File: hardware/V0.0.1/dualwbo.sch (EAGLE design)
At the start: 93 parts, among them IC1 AT90CAN128, IC10 ADS1015BQDGSRQ1, IC11 AD5337BRMZ, IC12 ADS1015BQDGSRQ1, IC2 AVR-JTAG, IC3 TJA1050, IC4 ADR01_02_03, IC5 TLS115B0EJXUMA1, IC6 TLE42754D, IC7 CJ125_QFP32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

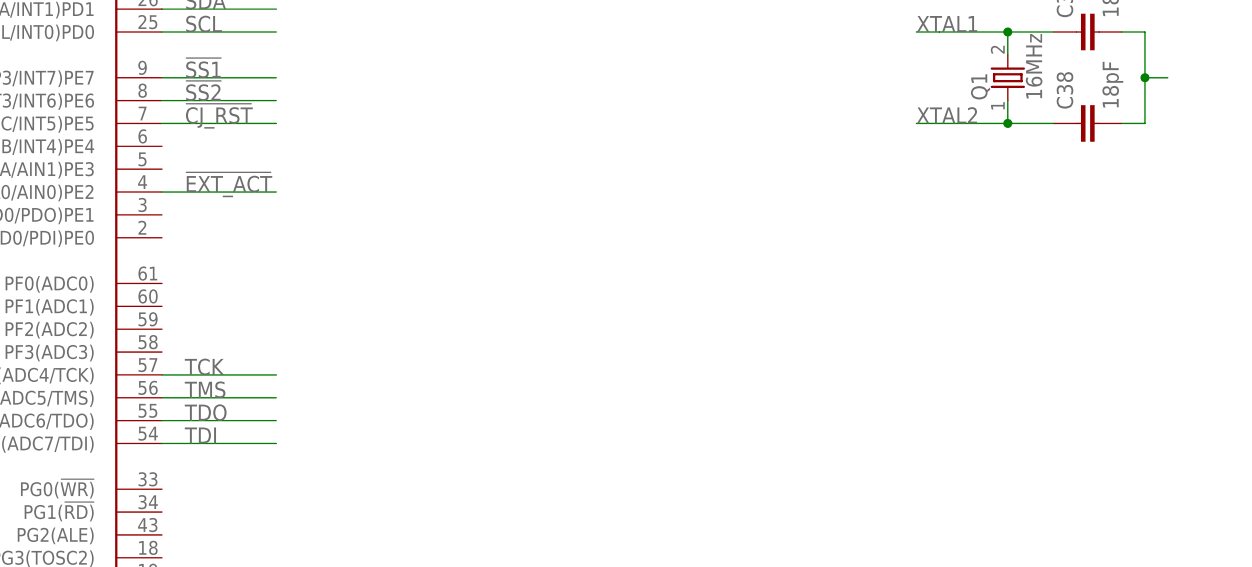
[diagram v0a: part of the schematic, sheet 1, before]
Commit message: uart added
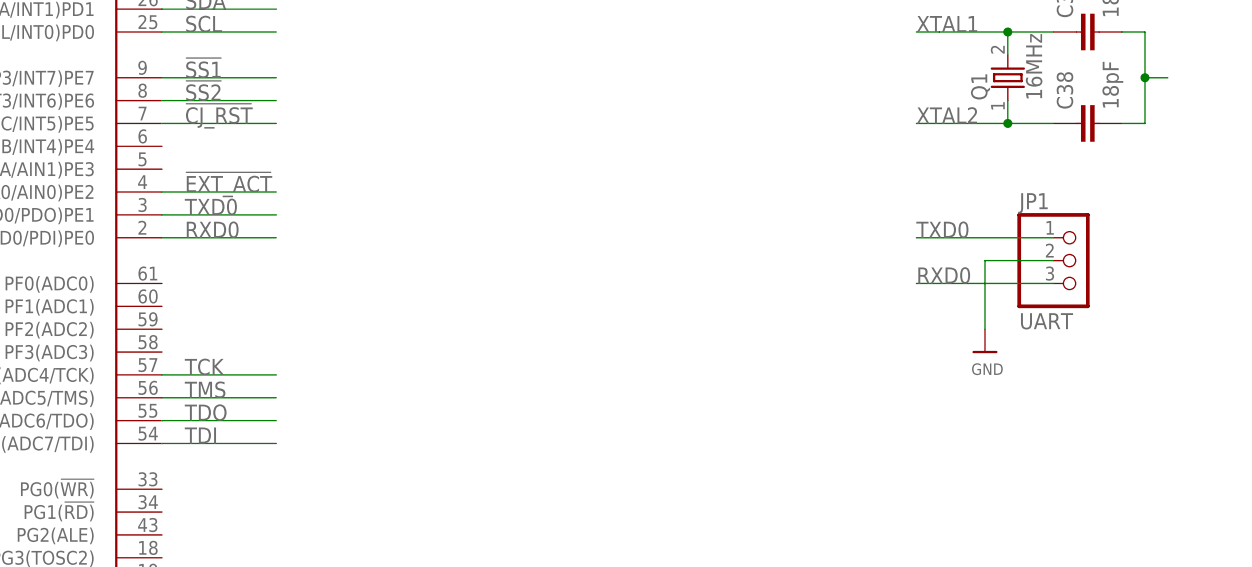
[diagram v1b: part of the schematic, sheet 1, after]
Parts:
- added JP1: UART, Heinrich:PINHD-1X3
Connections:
- new net RXD0: IC1.(RXD0/PDI)PE0, JP1.3
- new net TXD0: IC1.(TXD0/PDO)PE1, JP1.1
- net GND: now also JP1.2
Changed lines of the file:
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@@
 <part name="C40" library="rcl" library_urn="urn:adsk.eagle:library:334" deviceset="C-EU" device="C0805" package3d_urn="urn:adsk.eagle:package:23617/2" value="1uF"/>
 <part name="U$72" library="microbuilder" deviceset="AGND" device=""/>
+<part name="JP1" library="Heinrich" deviceset="PINHD-1X3" device="" value="UART"/>
+<part name="U$82" library="microbuilder" deviceset="GND" device=""/>
 </parts>
 <sheets>
@@
 <instance part="C6" gate="G$1" x="27.94" y="139.7"/>
 <instance part="U$77" gate="G$1" x="27.94" y="129.54"/>
+<instance part="JP1" gate="G$1" x="215.9" y="53.34"/>
+<instance part="U$82" gate="G$1" x="208.28" y="40.64"/>
 </instances>
 <busses>
@@
 <pinref part="U$4" gate="G$1" pin="GND"/>
 <wire x1="220.98" y1="121.92" x2="220.98" y2="119.38" width="0.1524" layer="91"/>
+</segment>
+<segment>
+<pinref part="JP1" gate="G$1" pin="2"/>
+<wire x1="215.9" y1="50.8" x2="208.28" y2="50.8" width="0.1524" layer="91"/>
+<wire x1="208.28" y1="50.8" x2="208.28" y2="43.18" width="0.1524" layer="91"/>
+<pinref part="U$82" gate="G$1" pin="GND"/>
 </segment>
 </net>
@@
 </segment>
 </net>
+<net name="TXD0" class="0">
+<segment>
+<pinref part="IC1" gate="G$1" pin="(TXD0/PDO)PE1"/>
+<wire x1="116.84" y1="55.88" x2="129.54" y2="55.88" width="0.1524" layer="91"/>
+<label x="119.38" y="55.88" size="1.778" layer="95"/>
+</segment>
+<segment>
+<pinref part="JP1" gate="G$1" pin="1"/>
+<wire x1="215.9" y1="53.34" x2="200.66" y2="53.34" width="0.1524" layer="91"/>
+<label x="200.66" y="53.34" size="1.778" layer="95"/>
+</segment>
+</net>
+<net name="RXD0" class="0">
+<segment>
+<pinref part="IC1" gate="G$1" pin="(RXD0/PDI)PE0"/>
+<wire x1="116.84" y1="53.34" x2="129.54" y2="53.34" width="0.1524" layer="91"/>
+<label x="119.38" y="53.34" size="1.778" layer="95"/>
+</segment>
+<segment>
+<pinref part="JP1" gate="G$1" pin="3"/>
+<wire x1="215.9" y1="48.26" x2="200.66" y2="48.26" width="0.1524" layer="91"/>
+<label x="200.66" y="48.26" size="1.778" layer="95"/>
+</segment>
+</net>

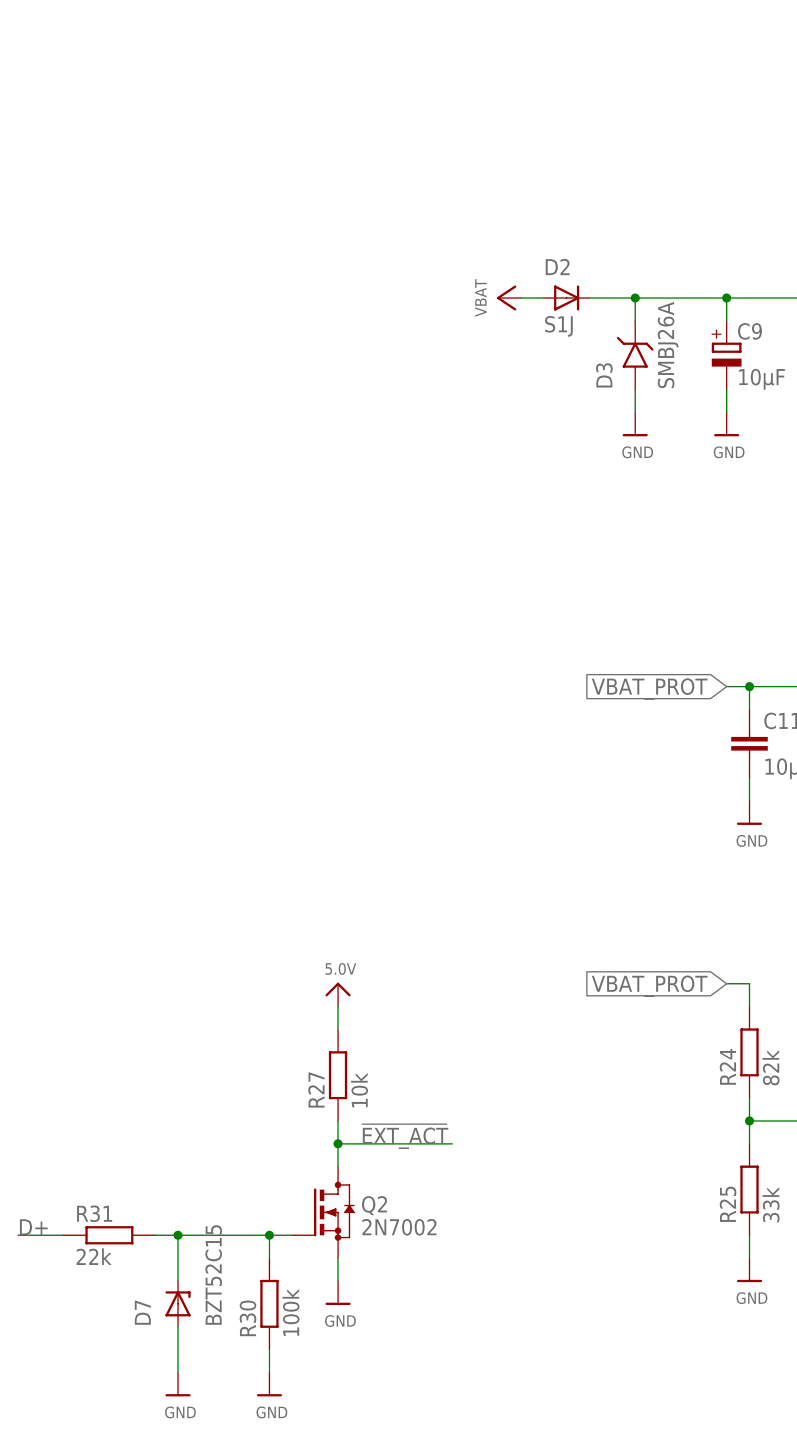
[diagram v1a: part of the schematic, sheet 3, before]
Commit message: Polarity protection revised
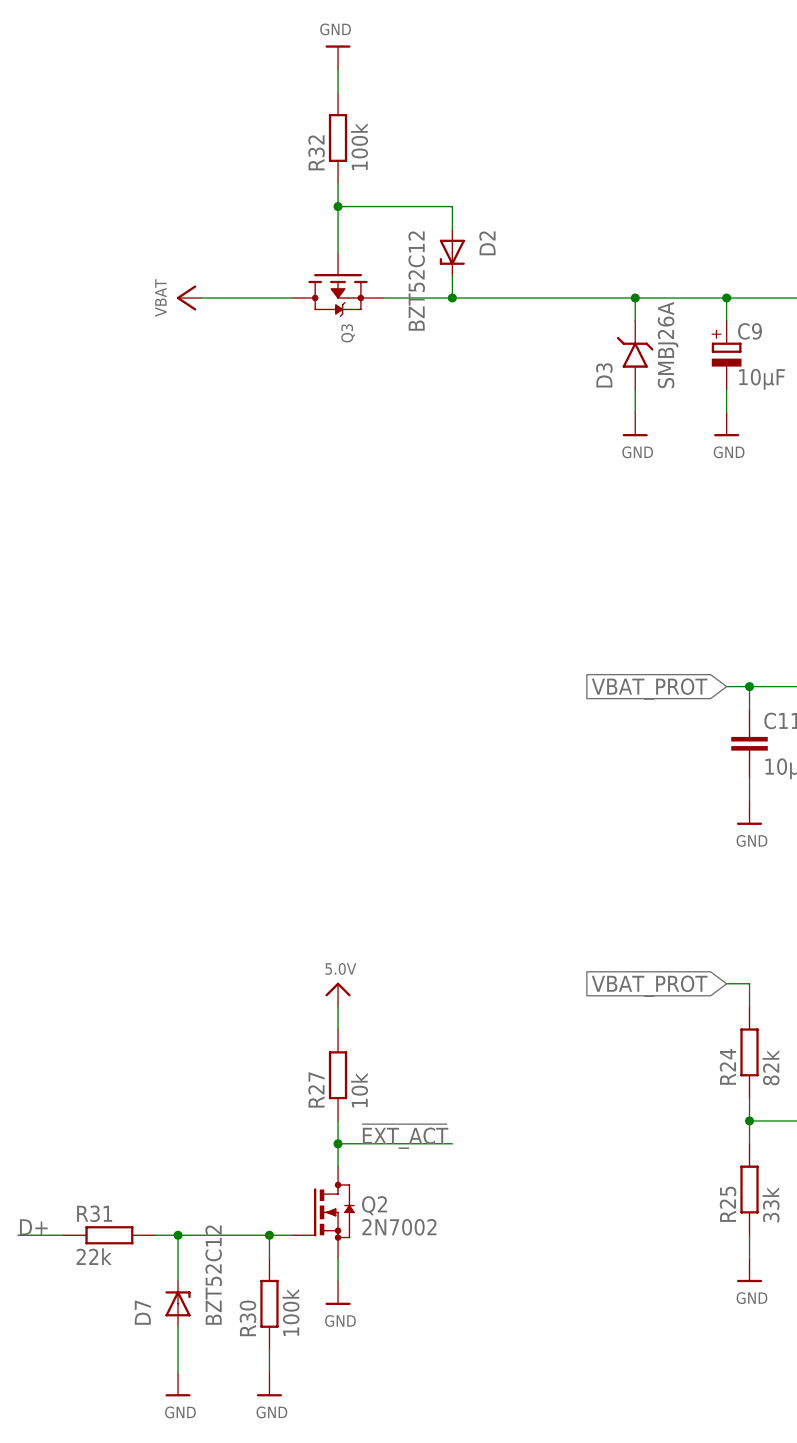
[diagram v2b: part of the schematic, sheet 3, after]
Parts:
- added Q3: (no value), microbuilder:MOSFET-P
- added R32: 100k, rcl:R-EU_R0805
- D2: value S1J -> BZT52C12; device Heinrich:DIODESMA -> Heinrich:Z-DIODESOD123
- D7: value BZT52C15 -> BZT52C12
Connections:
- new net N$32: D2.A, Q3.G, R32.1
- net ANALOG1: now also J1A.A11
- net ANALOG2: now also J1A.A2
- net CAN_H: now also J1A.A9
- net CAN_L: now also J1A.A4
- net D+: now also J1A.A8
- net GND: now also J1A.A1, J1A.A10, J1A.A12, J1A.A3, J1A.A5, J1A.A6, R32.2
- net VBAT: now also J1A.A7, Q3.D; no longer D2.A
- net VBAT_PROT: now also Q3.S
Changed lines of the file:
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@@
 <part name="U$21" library="microbuilder" deviceset="5.0V" device=""/>
 <part name="U$22" library="microbuilder" deviceset="GND" device=""/>
-<part name="D2" library="Heinrich" deviceset="DIODE" device="SMA" value="S1J"/>
 <part name="D3" library="Heinrich" deviceset="P6SMBXXA" device="SMB" value="SMBJ26A"/>
 <part name="C9" library="rcl" library_urn="urn:adsk.eagle:library:334" deviceset="CPOL-EU" device="D" package3d_urn="urn:adsk.eagle:package:23424/2" value="10µF"/>
@@
 <part name="U$80" library="microbuilder" deviceset="GND" device=""/>
 <part name="U$81" library="microbuilder" deviceset="GND" device=""/>
-<part name="D7" library="Heinrich" deviceset="Z-DIODE" device="SOD123" value="BZT52C15"/>
+<part name="D7" library="Heinrich" deviceset="Z-DIODE" device="SOD123" value="BZT52C12"/>
 <part name="C40" library="rcl" library_urn="urn:adsk.eagle:library:334" deviceset="C-EU" device="C0805" package3d_urn="urn:adsk.eagle:package:23617/2" value="1uF"/>
 <part name="U$72" library="microbuilder" deviceset="AGND" device=""/>
 <part name="JP1" library="Heinrich" deviceset="PINHD-1X3" device="" value="UART"/>
 <part name="U$82" library="microbuilder" deviceset="GND" device=""/>
+<part name="U$83" library="microbuilder" deviceset="GND" device=""/>
+<part name="U$84" library="Heinrich" deviceset="VBAT" device=""/>
+<part name="Q3" library="microbuilder" deviceset="MOSFET-P" device=""/>
+<part name="U$85" library="microbuilder" deviceset="GND" device=""/>
+<part name="R32" library="rcl" library_urn="urn:adsk.eagle:library:334" deviceset="R-EU_" device="R0805" package3d_urn="urn:adsk.eagle:package:23553/2" value="100k"/>
+<part name="D2" library="Heinrich" deviceset="Z-DIODE" device="SOD123" value="BZT52C12"/>
 </parts>
 <sheets>
@@
 <instance part="U$21" gate="G$1" x="160.02" y="139.7" rot="R270"/>
 <instance part="U$22" gate="G$1" x="157.48" y="121.92"/>
-<instance part="D2" gate="G$1" x="83.82" y="142.24"/>
 <instance part="D3" gate="G$1" x="91.44" y="137.16" rot="R90"/>
 <instance part="C9" gate="G$1" x="101.6" y="137.16"/>
@@
 <instance part="U$24" gate="G$1" x="101.6" y="127"/>
 <instance part="U$25" gate="G$1" x="91.44" y="127"/>
-<instance part="U$26" gate="G$1" x="78.74" y="142.24" rot="R90"/>
+<instance part="U$26" gate="G$1" x="43.18" y="142.24" rot="R90"/>
 <instance part="R1" gate="G$1" x="147.32" y="149.86" rot="R90"/>
 <instance part="U$27" gate="G$1" x="147.32" y="157.48"/>
@@
 <instance part="C40" gate="G$1" x="220.98" y="93.98"/>
 <instance part="U$72" gate="G$1" x="220.98" y="83.82"/>
+<instance part="Q3" gate="G$1" x="58.42" y="142.24" rot="R270"/>
+<instance part="U$85" gate="G$1" x="58.42" y="170.18" rot="R180"/>
+<instance part="R32" gate="G$1" x="58.42" y="160.02" rot="R90"/>
+<instance part="D2" gate="G$1" x="71.12" y="147.32" rot="R270"/>
 </instances>
 <busses>
@@
 <wire x1="40.64" y1="27.94" x2="40.64" y2="22.86" width="0.1524" layer="91"/>
 </segment>
+<segment>
+<pinref part="U$85" gate="G$1" pin="GND"/>
+<pinref part="R32" gate="G$1" pin="2"/>
+<wire x1="58.42" y1="167.64" x2="58.42" y2="165.1" width="0.1524" layer="91"/>
+</segment>
 </net>
 <net name="VBAT_PROT" class="0">
@@
 <pinref part="IC6" gate="G$1" pin="I"/>
 <wire x1="124.46" y1="142.24" x2="119.38" y2="142.24" width="0.1524" layer="91"/>
-<pinref part="D2" gate="G$1" pin="C"/>
-<wire x1="86.36" y1="142.24" x2="91.44" y2="142.24" width="0.1524" layer="91"/>
 <pinref part="C9" gate="G$1" pin="+"/>
 <wire x1="91.44" y1="142.24" x2="101.6" y2="142.24" width="0.1524" layer="91"/>
@@
 <pinref part="D3" gate="G$1" pin="C"/>
 <wire x1="91.44" y1="139.7" x2="91.44" y2="142.24" width="0.1524" layer="91"/>
-<junction x="91.44" y="142.24"/>
 <wire x1="111.76" y1="142.24" x2="111.76" y2="144.78" width="0.1524" layer="91"/>
 <label x="111.76" y="144.78" size="1.778" layer="95" rot="R90" xref="yes"/>
+<pinref part="Q3" gate="G$1" pin="S"/>
+<wire x1="63.5" y1="142.24" x2="71.12" y2="142.24" width="0.1524" layer="91"/>
+<junction x="91.44" y="142.24"/>
+<pinref part="D2" gate="G$1" pin="C"/>
+<wire x1="71.12" y1="142.24" x2="91.44" y2="142.24" width="0.1524" layer="91"/>
+<wire x1="71.12" y1="144.78" x2="71.12" y2="142.24" width="0.1524" layer="91"/>
+<junction x="71.12" y="142.24"/>
 </segment>
 <segment>
@@
 </segment>
 </net>
-<net name="VBAT" class="0">
-<segment>
-<pinref part="U$26" gate="G$1" pin="VBAT"/>
-<pinref part="D2" gate="G$1" pin="A"/>
-<wire x1="78.74" y1="142.24" x2="81.28" y2="142.24" width="0.1524" layer="91"/>
-</segment>
-</net>
 <net name="!RESET" class="0">
 <segment>
@@
 <label x="22.86" y="38.1" size="1.778" layer="95"/>
 <wire x1="25.4" y1="38.1" x2="22.86" y2="38.1" width="0.1524" layer="91"/>
+</segment>
+</net>
+<net name="VBAT" class="0">
+<segment>
+<pinref part="U$26" gate="G$1" pin="VBAT"/>
+<pinref part="Q3" gate="G$1" pin="D"/>
+<wire x1="43.18" y1="142.24" x2="53.34" y2="142.24" width="0.1524" layer="91"/>
+</segment>
+</net>
+<net name="N$32" class="0">
+<segment>
+<pinref part="R32" gate="G$1" pin="1"/>
+<pinref part="Q3" gate="G$1" pin="G"/>
+<wire x1="58.42" y1="154.94" x2="58.42" y2="152.4" width="0.1524" layer="91"/>
+<wire x1="58.42" y1="152.4" x2="58.42" y2="147.32" width="0.1524" layer="91"/>
+<wire x1="58.42" y1="152.4" x2="71.12" y2="152.4" width="0.1524" layer="91"/>
+<junction x="58.42" y="152.4"/>
+<pinref part="D2" gate="G$1" pin="A"/>
+<wire x1="71.12" y1="152.4" x2="71.12" y2="149.86" width="0.1524" layer="91"/>
 </segment>
 </net>
@@
 <instance part="J1" gate="A" x="40.64" y="134.62"/>
 <instance part="J1" gate="B" x="40.64" y="78.74"/>
+<instance part="U$83" gate="G$1" x="50.8" y="114.3"/>
+<instance part="U$84" gate="G$1" x="58.42" y="137.16" rot="R270"/>
 </instances>
 <busses>
 </busses>
 <nets>
+<net name="GND" class="0">
+<segment>
+<pinref part="J1" gate="A" pin="A1"/>
+<pinref part="U$83" gate="G$1" pin="GND"/>
+<wire x1="48.26" y1="121.92" x2="50.8" y2="121.92" width="0.1524" layer="91"/>
+<wire x1="50.8" y1="121.92" x2="50.8" y2="116.84" width="0.1524" layer="91"/>
+<pinref part="J1" gate="A" pin="A3"/>
+<wire x1="48.26" y1="127" x2="50.8" y2="127" width="0.1524" layer="91"/>
+<wire x1="50.8" y1="127" x2="50.8" y2="121.92" width="0.1524" layer="91"/>
+<junction x="50.8" y="121.92"/>
+<pinref part="J1" gate="A" pin="A5"/>
+<wire x1="48.26" y1="132.08" x2="50.8" y2="132.08" width="0.1524" layer="91"/>
+<wire x1="50.8" y1="132.08" x2="50.8" y2="127" width="0.1524" layer="91"/>
+<junction x="50.8" y="127"/>
+<pinref part="J1" gate="A" pin="A6"/>
+<wire x1="48.26" y1="134.62" x2="50.8" y2="134.62" width="0.1524" layer="91"/>
+<wire x1="50.8" y1="134.62" x2="50.8" y2="132.08" width="0.1524" layer="91"/>
+<junction x="50.8" y="132.08"/>
+<pinref part="J1" gate="A" pin="A10"/>
+<wire x1="48.26" y1="144.78" x2="50.8" y2="144.78" width="0.1524" layer="91"/>
+<wire x1="50.8" y1="144.78" x2="50.8" y2="134.62" width="0.1524" layer="91"/>
+<junction x="50.8" y="134.62"/>
+<pinref part="J1" gate="A" pin="A12"/>
+<wire x1="48.26" y1="149.86" x2="50.8" y2="149.86" width="0.1524" layer="91"/>
+<wire x1="50.8" y1="149.86" x2="50.8" y2="144.78" width="0.1524" layer="91"/>
+<junction x="50.8" y="144.78"/>
+</segment>
+</net>
+<net name="D+" class="0">
+<segment>
+<pinref part="J1" gate="A" pin="A8"/>
+<wire x1="48.26" y1="139.7" x2="58.42" y2="139.7" width="0.1524" layer="91"/>
+<label x="53.34" y="139.7" size="1.778" layer="95"/>
+</segment>
+</net>
+<net name="VBAT" class="0">
+<segment>
+<pinref part="J1" gate="A" pin="A7"/>
+<wire x1="48.26" y1="137.16" x2="58.42" y2="137.16" width="0.1524" layer="91"/>
+<pinref part="U$84" gate="G$1" pin="VBAT"/>
+</segment>
+</net>
+<net name="ANALOG2" class="0">
+<segment>
+<pinref part="J1" gate="A" pin="A2"/>
+<wire x1="48.26" y1="124.46" x2="58.42" y2="124.46" width="0.1524" layer="91"/>
+<label x="53.34" y="124.46" size="1.778" layer="95"/>
+</segment>
+</net>
+<net name="ANALOG1" class="0">
+<segment>
+<pinref part="J1" gate="A" pin="A11"/>
+<wire x1="48.26" y1="147.32" x2="58.42" y2="147.32" width="0.1524" layer="91"/>
+<label x="53.34" y="147.32" size="1.778" layer="95"/>
+</segment>
+</net>
+<net name="CAN_L" class="0">
+<segment>
+<pinref part="J1" gate="A" pin="A4"/>
+<wire x1="48.26" y1="129.54" x2="58.42" y2="129.54" width="0.1524" layer="91"/>
+<label x="53.34" y="129.54" size="1.778" layer="95"/>
+</segment>
+</net>
+<net name="CAN_H" class="0">
+<segment>
+<pinref part="J1" gate="A" pin="A9"/>
+<wire x1="48.26" y1="142.24" x2="58.42" y2="142.24" width="0.1524" layer="91"/>
+<label x="53.34" y="142.24" size="1.778" layer="95"/>
+</segment>
+</net>
 </nets>
 </sheet>
